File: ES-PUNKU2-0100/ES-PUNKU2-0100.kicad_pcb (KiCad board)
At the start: 2 copper layers, 60 parts, among them J1 PROGRAMACION, J10 ALARMA, J11 SERIAL, J2 12VDC, J3 BOOT, J4 Micro_SD_Card, J5 PULSADOR, J6 Conn_01x02, J7 SENSOR, J8 RFID, J9 CONF, K1 RELE, Q1 BC817, Q2 IRF7309IPBF, Q3 IRF7309IPBF, Q4 BC817, Q5 2N7002P, Q6 2N7002P, Q7 2N7002P, SW1 RESET, U1 LM2575, U2 ESP32-WROOM-32D, U3 LD1117S33CTR, U4 MCP7940N, U5 LTV-816S, U6 LTV-816S, Y1 32,768KHz

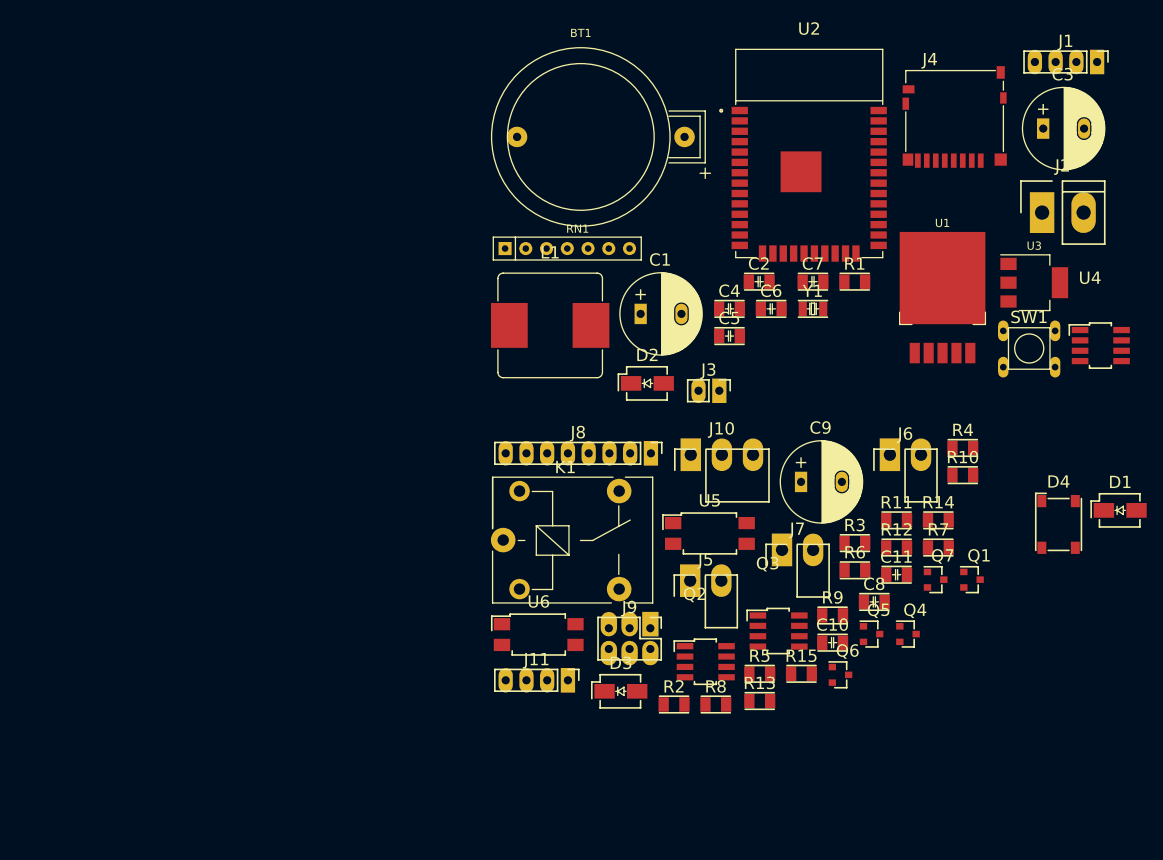
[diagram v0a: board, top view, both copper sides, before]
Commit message: Incorporación de las correcciones sugeridas por Martin Ribelotta y posicionamiento de componentes
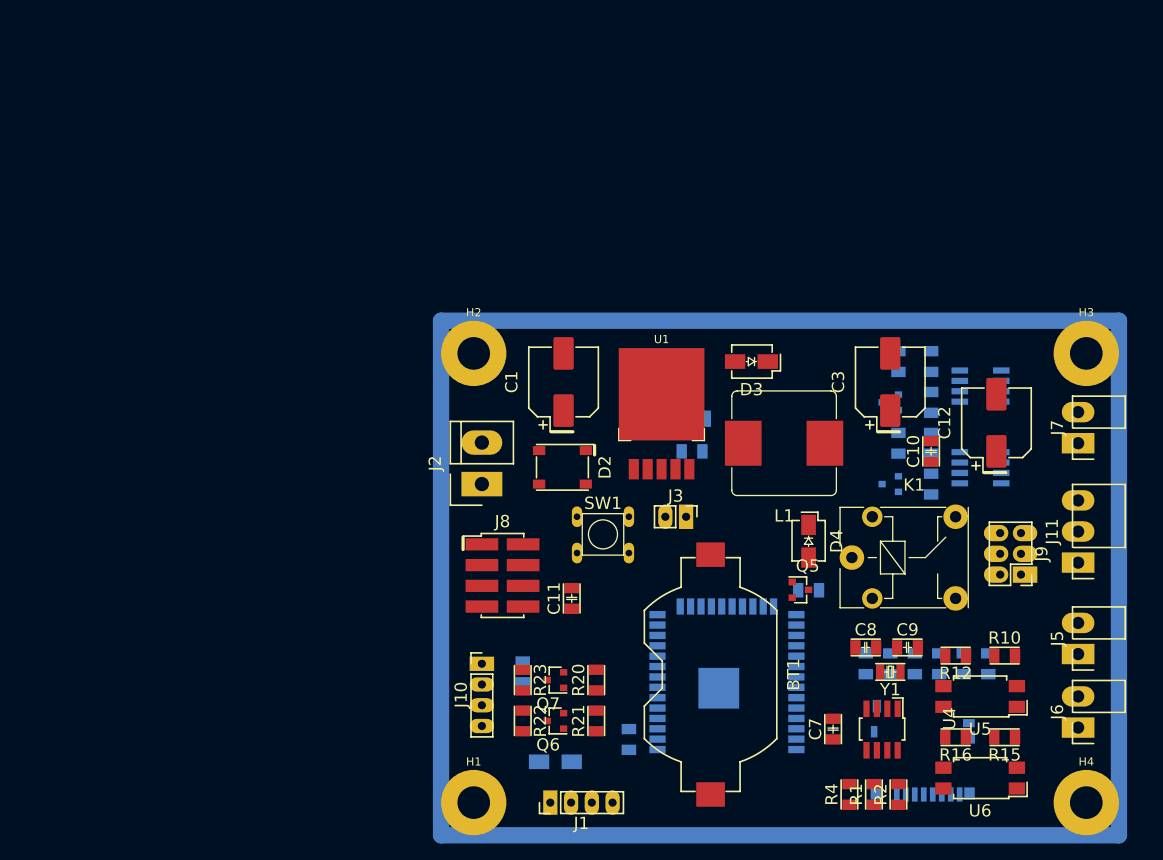
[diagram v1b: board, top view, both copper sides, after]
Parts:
- removed the C11 at (156.8, 117.1)
- removed the C4 at (136.3, 84.5)
- removed the D3 at (123.0, 131.4)
- removed the J10 at (131.6, 102.4)
- removed the J6 at (156.0, 102.4)
- removed the R12 at (156.8, 113.8)
- removed the R4 at (164.9, 101.6)
- removed RN1: 10K, Resistor_THT:R_Array_SIP7
- added C12: 470uF, encapsulados:CP_Elec_8x10, F.Cu at (169.0, 98.5)
- added C13: 100nF, encapsulados:C_1206_0805_Dual, B.Cu at (111.0, 129.0)
- added C5: 100nF, encapsulados:C_1206_0805_Dual, B.Cu at (125.0, 97.0)
- added C8: 10pF, encapsulados:C_1206_0805_Dual, F.Cu at (153.0, 126.0)
- added D2: CD-MBL206SL, encapsulados:BOURNS-0.23x0.20, F.Cu at (115.9, 104.0)
- added H1: MountingHole_Pad, MountingHole:MountingHole_4mm_Pad, F.Cu at (105.0, 145.0)
- added H2: MountingHole_Pad, MountingHole:MountingHole_4mm_Pad, F.Cu at (105.0, 90.0)
- added H3: MountingHole_Pad, MountingHole:MountingHole_4mm_Pad, F.Cu at (180.0, 90.0)
- added H4: MountingHole_Pad, MountingHole:MountingHole_4mm_Pad, F.Cu at (180.0, 145.0)
- added J11: ALARMA, encapsulados:Bornera_Angulo_3_0.150_Inch, F.Cu at (179.0, 115.6)
- added J7: Conn_01x02, encapsulados:Bornera_Angulo_2_0.150_Inch, F.Cu at (179.0, 101.0)
- added R1: 2K2, encapsulados:R_1206_0805_Dual, F.Cu at (154.0, 144.0)
- added R17: 1K, encapsulados:R_1206_0805_Dual, B.Cu at (161.0, 91.0)
- added R2: 2K2, encapsulados:R_1206_0805_Dual, F.Cu at (157.0, 144.0)
- added R20: 10K, encapsulados:R_1206_0805_Dual, F.Cu at (120.0, 130.0)
- added R21: 10K, encapsulados:R_1206_0805_Dual, F.Cu at (120.0, 135.0)
- added R3: 10K, encapsulados:R_1206_0805_Dual, B.Cu at (168.0, 128.0)
- added R5: 10K, encapsulados:R_1206_0805_Dual, B.Cu at (165.0, 128.0)
- added R6: 10K, encapsulados:R_1206_0805_Dual, B.Cu at (162.0, 128.0)
- added R7: 10K, encapsulados:R_1206_0805_Dual, B.Cu at (159.0, 128.0)
- added R9: 10K, encapsulados:R_1206_0805_Dual, B.Cu at (153.0, 128.0)
- BT1: footprint encapsulados:CR2032_Horizontal -> encapsulados:BatteryHolder_Keystone_1058_1x2032
- C1, C3: footprint encapsulados:CP_Radial_D10_L20_P5 -> encapsulados:CP_Elec_8x10
- C2, C6, D1, J4, Q1, Q2, Q3, Q4, U2: moved to B.Cu
- C4: renamed from C5; moved to B.Cu
- C9: value 470uF -> 10pF; footprint encapsulados:CP_Radial_D10_L20_P5 -> encapsulados:C_1206_0805_Dual
- D4: value CD-MBL206SL -> SK210TR; footprint encapsulados:BOURNS-0.23x0.20 -> encapsulados:DO-214AA
- J8: footprint encapsulados:Pin_Header_Straight_1x08_Pitch2.54mm -> encapsulados:PinHeader_2x04_P2.54mm_Vertical_SMD
- K1: footprint encapsulados:Relay_NT73_Series_Form_C -> encapsulados:Relay_NT78_Series_Form_C
- R11: renamed from R2; moved to B.Cu
- R13: value 10K -> 1K; moved to B.Cu
- R14: renamed from R5; moved to B.Cu
- R18: renamed from R9; moved to B.Cu
- R19: renamed from R11; moved to B.Cu
- R8: value 1K -> 10K; moved to B.Cu
- U1: value LM2575 -> LM2575S5
- U3: value LD1117S33CTR -> LD1117S33; moved to B.Cu
- moved J1 112.7 mm to (114.4, 145.0), turned to 180 degrees
- moved J4 77.8 mm to (164.5, 143.1), turned to 180 degrees
- moved J2 76.2 mm to (106.0, 106.0), turned to 90 degrees
- moved D1 75.7 mm to (115.0, 140.0)
- moved U2 68.5 mm to (136.0, 133.2)
- moved BT1 65.9 mm to (134.0, 129.3), turned to 270 degrees
- moved R4 62.8 mm to (151.0, 144.0), turned to 90 degrees
- moved C2 58.3 mm to (124.0, 137.3), turned to 270 degrees
- moved SW1 56.9 mm to (117.7, 110.0)
- moved U6 56.8 mm to (167.0, 142.0), turned to 180 degrees
- moved R22 56.5 mm to (111.0, 135.0), turned to 270 degrees
- moved C7 54.8 mm to (149.0, 136.0), turned to 90 degrees
- moved U4 54.0 mm to (155.0, 136.0), turned to 270 degrees
- moved J5 48.3 mm to (179.0, 126.8), turned to 90 degrees
- moved Q7 48.2 mm to (115.0, 130.0), turned to 180 degrees
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- renumbered C8 to C10, C10 to C11, D2 to D3, J11 to J10, J7 to J6, R3 to R10, R6 to R12, R7 to R15, R10 to R16, R14 to R22, R15 to R23, R1 to R4
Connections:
- C9 pad 1: +12V -> Net-(C9-Pad1)
- D4 pad 1: GND -> +12V
- J2 pad 1: Net-(D4-Pad4) -> Net-(D2-Pad4)
- J2 pad 2: Net-(D4-Pad2) -> Net-(D2-Pad2)
- K1 pad 2: +12V -> Net-(D4-Pad2)
- K1 pad 5: Net-(D3-Pad2) -> +12V
- Q5 pad 3: Net-(D3-Pad2) -> Net-(D4-Pad2)
- R13 pad 1: +3V3 -> +12V
- R13 pad 2: /Perifericos/SCI_TXD -> Net-(Q1-Pad3)
- R8 pad 1: +12V -> +3V3
- R8 pad 2: Net-(Q3-Pad2) -> /Procesador/SD_CS
- U4 pad 1: Net-(U4-Pad1) -> Net-(C9-Pad1)
- Y1 pad 1: Net-(U4-Pad1) -> Net-(C9-Pad1)
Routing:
- net Net-(D4-Pad2): track 0.00 -> 292.0 mm

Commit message: Primera versión ruteada de la placa
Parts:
- removed SW1: RESET, encapsulados:TACT_SWITCH
- added D5: SK210TR, encapsulados:DO-214AA, F.Cu at (114.5, 97.8)
- C13, D1, R3, R5, R6, R7, R8, R9: moved to F.Cu
- C7, C8, C9, R1, R10, R12, R15, R16, R2, R4, U4, U5, U6, Y1: moved to B.Cu
- J7: value Conn_01x02 -> CERRADURA
- moved U2 81.9 mm to (56.8, 112.5), turned to 270 degrees
- moved C2 80.3 mm to (52.8, 100.2), turned to 0 degrees
- moved J1 80.1 mm to (53.0, 93.5)
- moved J4 75.6 mm to (90.7, 126.8)
- moved C4 74.7 mm to (71.5, 124.0)
- moved R3 74.0 mm to (94.0, 127.5), turned to 90 degrees
- moved R5 74.0 mm to (91.0, 127.5), turned to 90 degrees
- moved R6 74.0 mm to (88.0, 127.5), turned to 90 degrees
- moved R7 74.0 mm to (85.0, 127.5), turned to 90 degrees
- moved R8 74.0 mm to (82.0, 127.5), turned to 90 degrees
- moved R9 74.0 mm to (79.0, 127.5), turned to 90 degrees
- moved C3 67.3 mm to (90.2, 79.0)
- moved D1 65.8 mm to (68.5, 93.5), turned to 180 degrees
- moved J3 63.4 mm to (70.2, 128.0), turned to 180 degrees
- moved R1 61.0 mm to (103.0, 110.5), turned to 270 degrees
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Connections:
- C2 pad 1: Net-(C2-Pad1) -> GND
- C2 pad 2: GND -> Net-(C2-Pad2)
- U2 pad 10: /Perifericos/DIRECTA -> /Perifericos/SENSOR
- U2 pad 11: /Perifericos/INVERSA -> /Procesador/I2C_SDA
- U2 pad 12: /Perifericos/ALARMA -> /Procesador/I2C_SCL
- U2 pad 3: Net-(C2-Pad1) -> Net-(C2-Pad2)
- U2 pad 6: /Perifericos/PULSADOR -> /Perifericos/INVERSA
- U2 pad 7: /Perifericos/SENSOR -> /Perifericos/DIRECTA
- U2 pad 8: /Procesador/I2C_SCL -> /Perifericos/ALARMA
- U2 pad 9: /Procesador/I2C_SDA -> /Perifericos/PULSADOR
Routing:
- net GND: track 0.00 -> 695.4 mm, vias 0 -> 9
- net Net-(D4-Pad2): track 292.0 -> 13.4 mm
- net +3V3: track 0.00 -> 270.2 mm, vias 0 -> 9
- net +12V: track 0.00 -> 212.5 mm, vias 0 -> 2
- net +5V: track 0.00 -> 90.2 mm, vias 0 -> 2
- net /Perifericos/DIRECTA: track 0.00 -> 83.4 mm
- net /Perifericos/SENSOR: track 0.00 -> 77.1 mm, vias 0 -> 2
- net /Perifericos/INVERSA: track 0.00 -> 76.5 mm
- net /Perifericos/PULSADOR: track 0.00 -> 70.8 mm, vias 0 -> 2
- net /Procesador/I2C_SDA: track 0.00 -> 60.7 mm, vias 0 -> 2
- net /Procesador/I2C_SCL: track 0.00 -> 53.2 mm, vias 0 -> 2
- net Net-(D3-Pad1): track 0.00 -> 52.4 mm
- net /Procesador/SD_CLK: track 0.00 -> 44.6 mm, vias 0 -> 1
- net /Perifericos/SCI_RXD: track 0.00 -> 42.5 mm, vias 0 -> 1
- net /Perifericos/ALARMA: track 0.00 -> 39.7 mm, vias 0 -> 1
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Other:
- board outline added: 87 x 66 mm
- net class Default: clearance 0.2 -> 0.3; trace_width 0.25 -> 0.5; via_dia 0.8 -> 1; via_drill 0.4 -> 0.5
- net class Delgadas added: clearance 0.3, trace_width 0.3, via_dia 1, via_drill 0.5
- net class Potencia added: clearance 0.3, trace_width 1, via_dia 1, via_drill 0.5
- rule trace_clearance: 0.2 -> 0.3
- rule trace_min: 0.2 -> 0.3
- rule via_min_drill: 0.3 -> 0.5
- rule via_min_size: 0.4 -> 1
- board text added: "Ancho mínimo de pista 0,3mm Separacion mínima entre señales 0,3mm Diametro mínimo de via 1mm Perforación mínima de via 0,5m Material de fabricación FR-4 de 1,6mm Espezor de cobre 35um / 1oz Doble faz con orificios metalizados Terminación superficial SnPb HASL"
- board text added: "EQUISER"
- board text added: "EQUISER IND.ARGENTINA TUCUMAN 2019"
- board text added: "Grilla de Posicionamiento: Principal 0,5mm Alternativa 0,25mm Gruilla de Ruteo: Principal 0,5mm Alternativa 0,25mm"
- board text added: "Información de diseño"
- board text added: "Información de fabricación"
- board text added: "PUNKU 1.00"

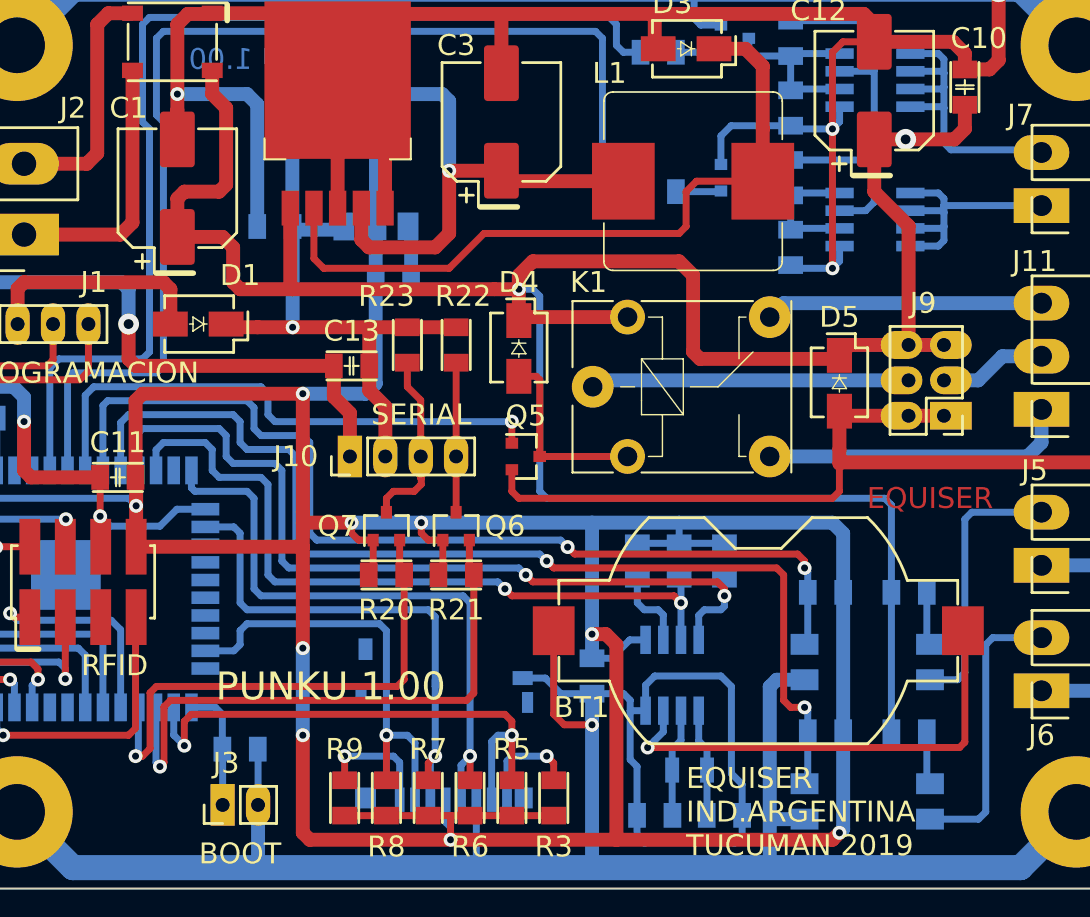
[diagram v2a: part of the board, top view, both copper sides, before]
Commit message: Correcciónes y exportacion del modelo 3D de la placa
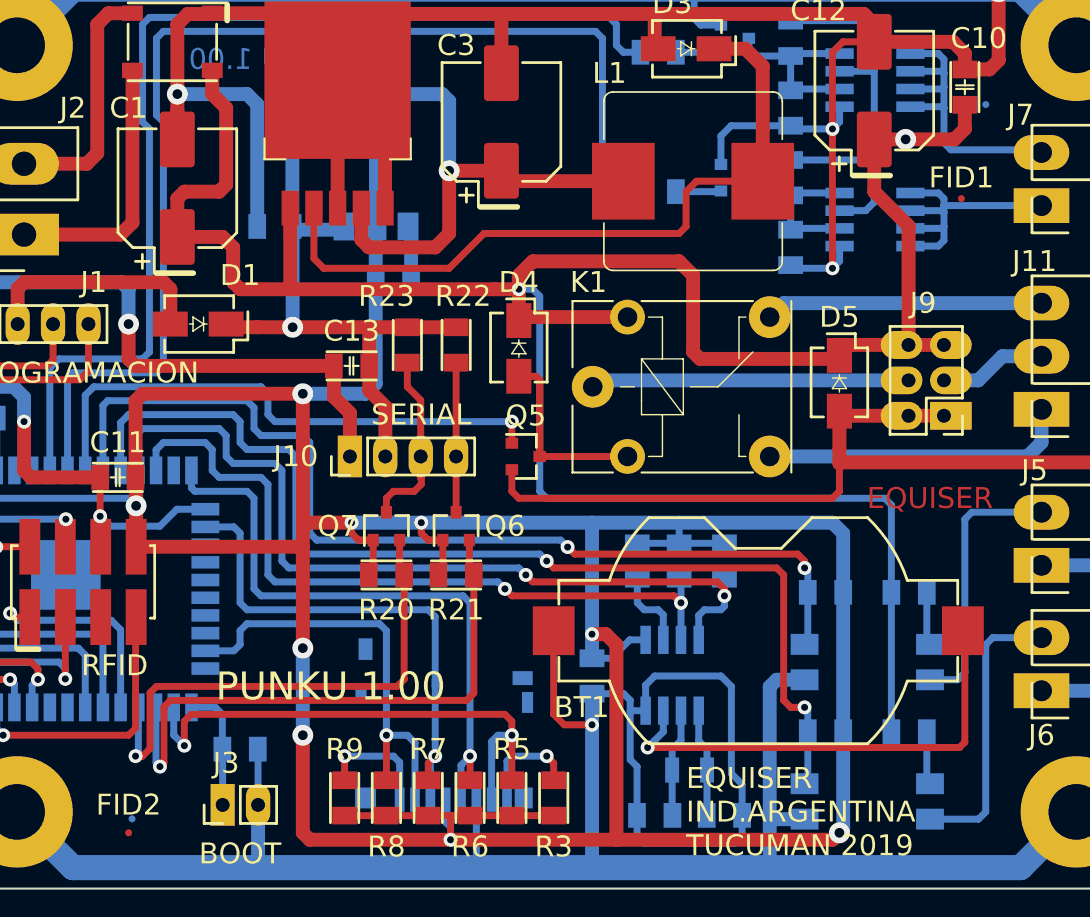
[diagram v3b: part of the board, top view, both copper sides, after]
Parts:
- added FID1: Fiducial, Fiducial:Fiducial_0.5mm_Mask1mm, F.Cu at (123.2, 84.5)
- added FID2: Fiducial, Fiducial:Fiducial_0.5mm_Mask1mm, F.Cu at (63.5, 130.0)
- added FID3: Fiducial, Fiducial:Fiducial_0.5mm_Mask1mm, B.Cu at (125.0, 77.8)
- added FID4: Fiducial, Fiducial:Fiducial_0.5mm_Mask1mm, B.Cu at (63.8, 129.0)
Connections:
- J4 pad 9: GND -> (no net)
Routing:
- net GND: track 695.4 -> 690.0 mm
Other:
- net class Default: via_dia 1 -> 1.5; via_drill 0.5 -> 0.7
- board text added: "Grilla de posicionamiento: Principal 0,5mm Alternativa 0,25mm Gruilla de ruteo: Principal 0,5mm Alternativa 0,25mm Base para las restricciones Ernesto Mayer, Estandar 10 mils"
- board text removed: "Grilla de Posicionamiento: Principal 0,5mm Alternativa 0,25mm Gruilla de Ruteo: Principal 0,5mm Alternativa 0,25mm"

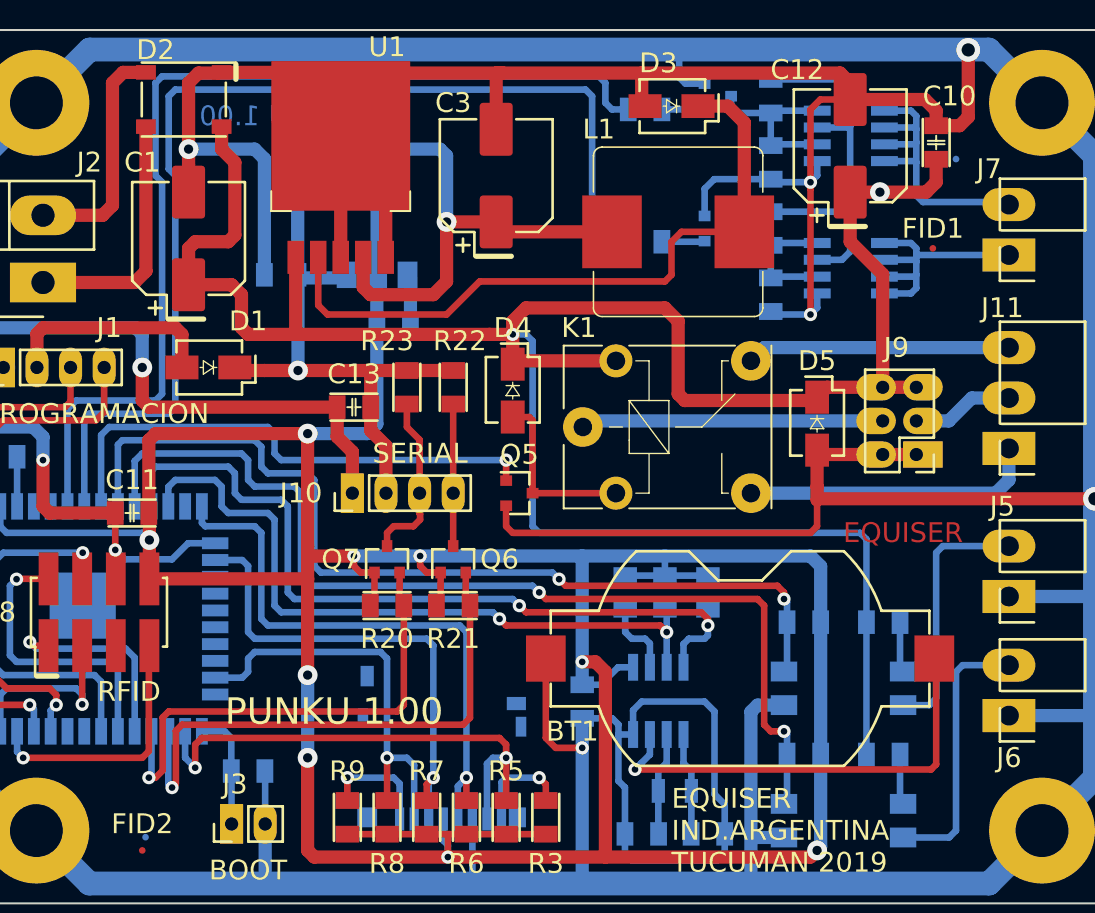
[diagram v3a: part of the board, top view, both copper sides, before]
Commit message: Correcciones de ruteo y agregado de una protección para la salida del puente H
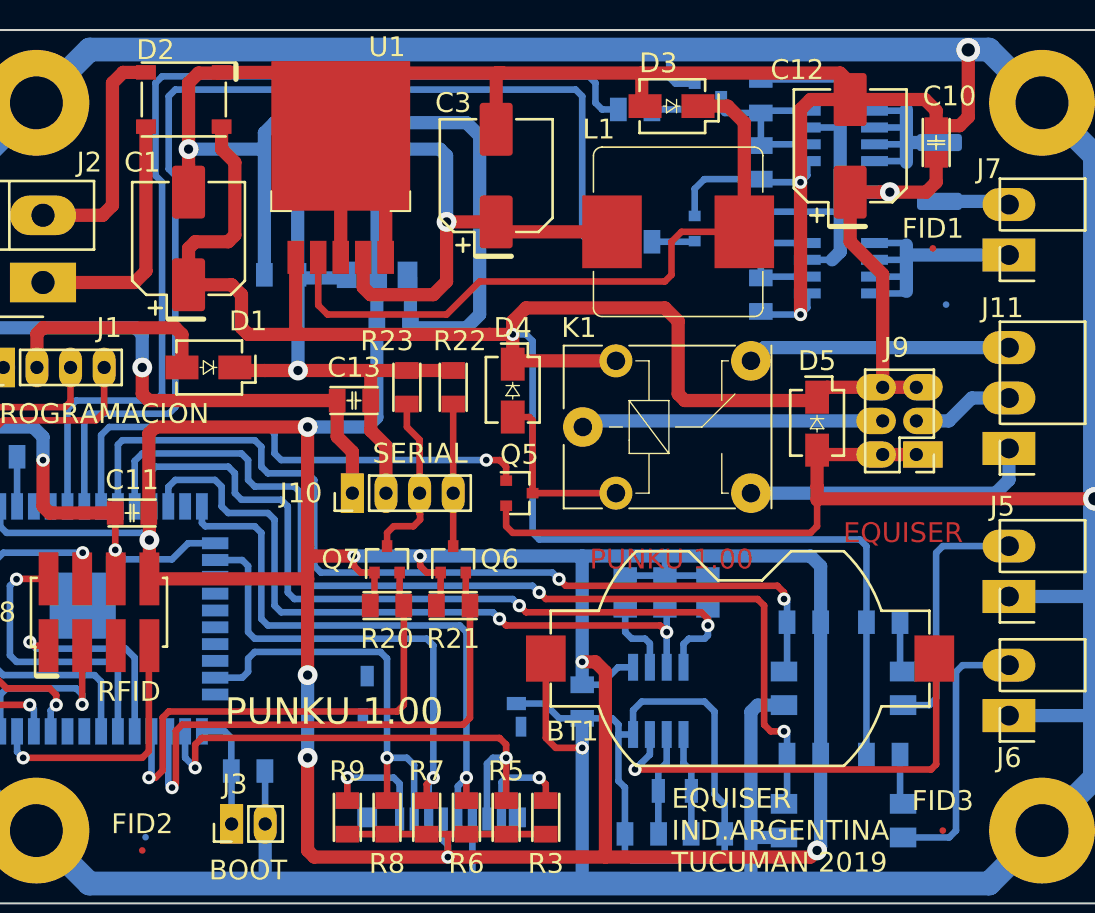
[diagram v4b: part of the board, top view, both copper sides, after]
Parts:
- added F1: Polyfuse, Resistor_SMD:R_1812_4532Metric_Pad1.30x3.40mm_HandSolder, B.Cu at (123.8, 78.7)
- added FID5: Fiducial, Fiducial:Fiducial_0.5mm_Mask1mm, B.Cu at (61.5, 76.0)
- added FID6: Fiducial, Fiducial:Fiducial_0.5mm_Mask1mm, B.Cu at (124.2, 88.8)
- FID3: moved to F.Cu
- moved FID3 50.8 mm to (124.0, 128.5), turned to 0 degrees
- moved Q1 0.75 mm to (106.2, 83.0)
- moved Q2 0.75 mm to (116.2, 86.0)
- moved Q3 0.75 mm to (116.2, 76.0)
- moved Q4 0.75 mm to (106.2, 73.0)
- moved R11 0.75 mm to (100.8, 84.0)
- moved R13 0.75 mm to (110.2, 83.0)
- moved R14 0.75 mm to (110.2, 88.0)
- moved R17 0.75 mm to (110.2, 73.0)
- moved R18 0.75 mm to (110.2, 78.0)
- moved R19 0.75 mm to (100.8, 74.0)
- moved C13 0.50 mm to (79.5, 96.0)
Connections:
- J4 pad 9: (no net) -> GND
- J7 pad 2: Net-(J7-Pad2) -> Net-(F1-Pad2)
- Q3 pad 5: Net-(J7-Pad2) -> Net-(F1-Pad1)
- Q3 pad 6: Net-(J7-Pad2) -> Net-(F1-Pad1)
- Q3 pad 7: Net-(J7-Pad2) -> Net-(F1-Pad1)
- Q3 pad 8: Net-(J7-Pad2) -> Net-(F1-Pad1)
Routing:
- net GND: track 690.0 -> 738.2 mm
- net Net-(J7-Pad2): track 23.2 -> 0.00 mm
- net Net-(F1-Pad1): track 0.00 -> 16.3 mm
- net Net-(F1-Pad2): track 0.00 -> 5.62 mm
- net +12V: track 212.5 -> 214.1 mm
- net Net-(J7-Pad1): track 20.1 -> 21.0 mm
- net /Perifericos/DIRECTA: track 83.4 -> 82.7 mm
- net /Perifericos/INVERSA: track 76.5 -> 75.8 mm
